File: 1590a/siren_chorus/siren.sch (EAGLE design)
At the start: 52 parts, among them IC1 NE5532, Q1 2N5457

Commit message: finished chorus and tremolo baords; other tweaks & polish
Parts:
- removed LED: PADSQR, supply pins:PADSQR
- added L+: PADSQR, supply pins:PADSQR
- added PAD1: PAD, supply pins:PAD
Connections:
- net LED: now also L+.P$1; no longer LED.P$1
- net VC: now also PAD1.P$1
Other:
- note added: "PT2399 CHORUS based on the madbean pedals glam (c)2016 burr settles"
- note added: "SIREN"
- moved on the sheet: 9V, BIAS, C1, C10, C11, C12, C13, C14, C15, C16, C17, C18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

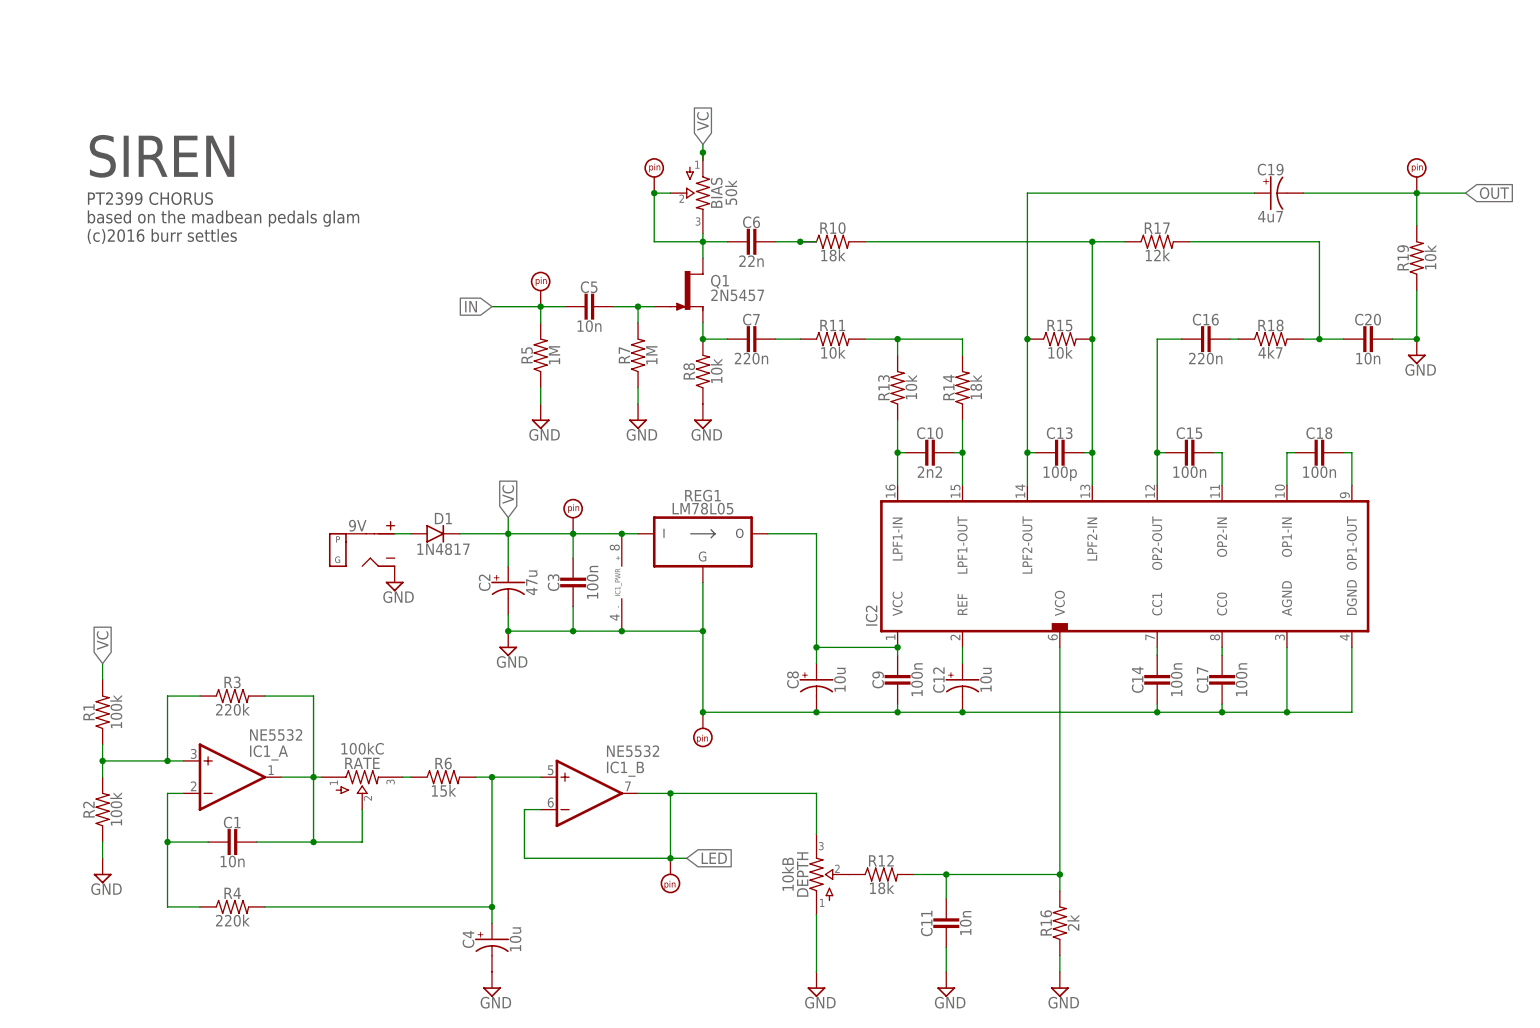
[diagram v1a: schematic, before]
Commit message: prettified schematics a bit
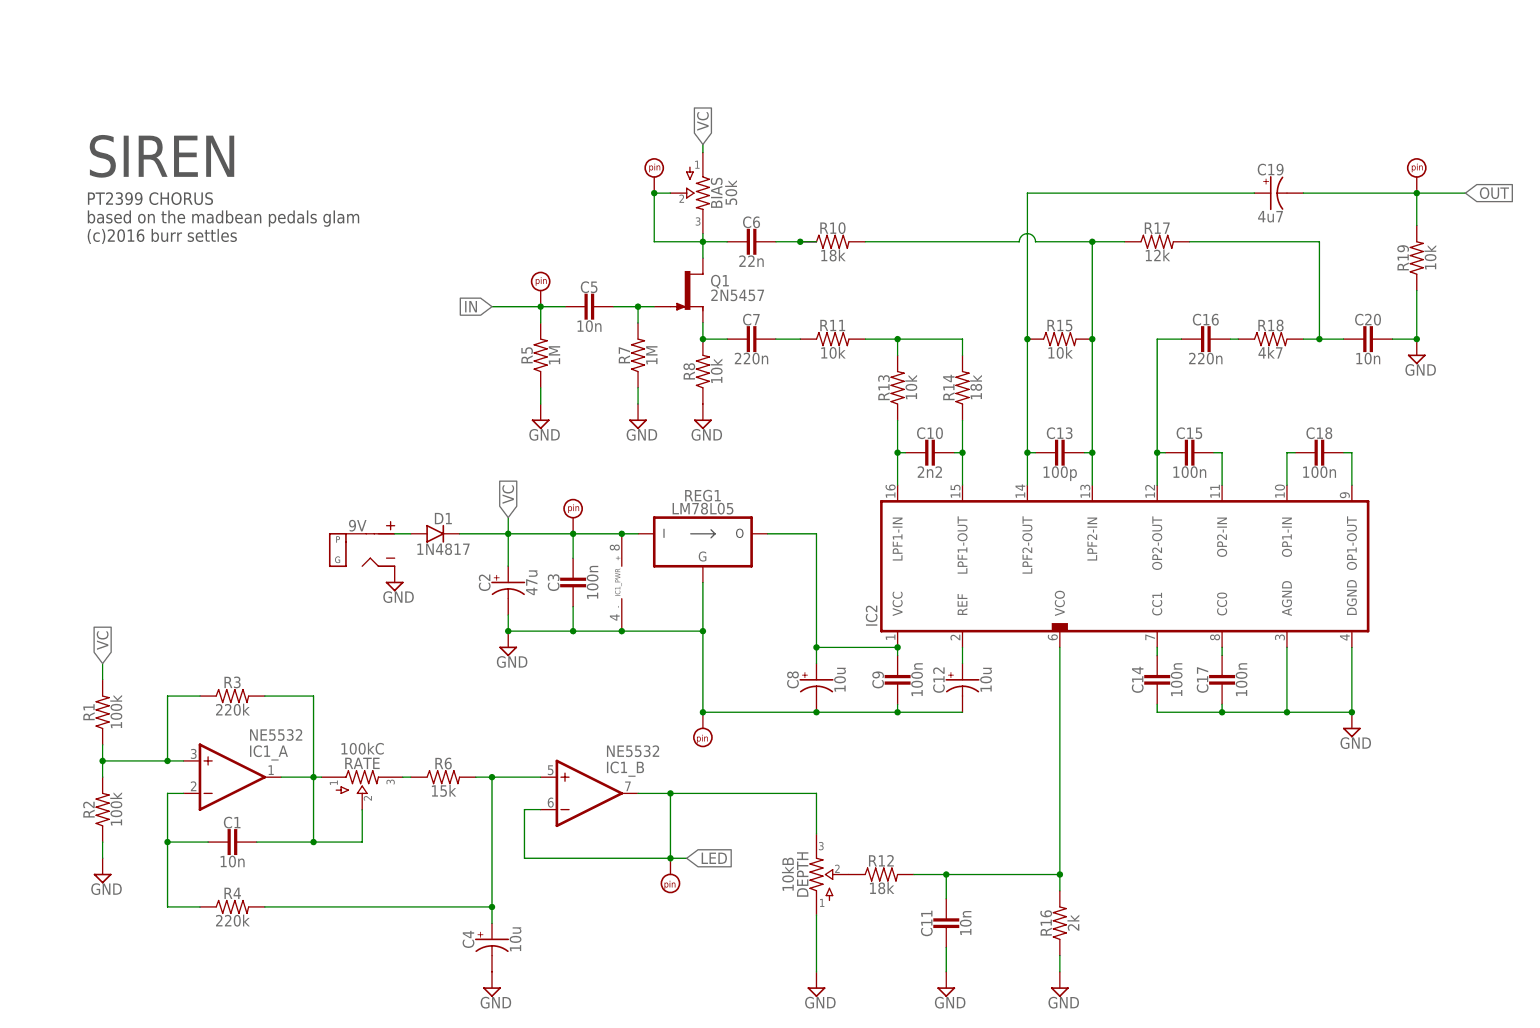
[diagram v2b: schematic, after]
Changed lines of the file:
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@@
 <setting verticaltext="up"/>
 </settings>
-<grid distance="0.1" unitdist="inch" unit="inch" style="lines" multiple="1" display="no" altdistance="0.01" altunitdist="inch" altunit="inch"/>
+<grid distance="0.05" unitdist="inch" unit="inch" style="lines" multiple="2" display="no" altdistance="0.01" altunitdist="inch" altunit="inch"/>
 <layers>
 <layer number="1" name="Top" color="4" fill="1" visible="no" active="no"/>
@@
 <part name="L+" library="supply pins" deviceset="PAD" device="SQR"/>
 <part name="PAD1" library="supply pins" deviceset="PAD" device=""/>
+<part name="GND8" library="supply pins" deviceset="GND" device=""/>
 </parts>
 <sheets>
@@
 <instance part="L+" gate="G$1" x="96.52" y="27.94" rot="R180"/>
 <instance part="PAD1" gate="G$1" x="81.28" y="78.74"/>
+<instance part="GND8" gate="GND" x="203.2" y="48.26"/>
 </instances>
 <busses>
@@
 <pinref part="C9" gate="G$1" pin="2"/>
 <wire x1="132.08" y1="52.07" x2="132.08" y2="50.8" width="0.1524" layer="91"/>
-<pinref part="IC2" gate="G$1" pin="DGND"/>
-<wire x1="142.24" y1="50.8" x2="172.72" y2="50.8" width="0.1524" layer="91"/>
-<wire x1="172.72" y1="50.8" x2="182.88" y2="50.8" width="0.1524" layer="91"/>
-<wire x1="182.88" y1="50.8" x2="193.04" y2="50.8" width="0.1524" layer="91"/>
-<wire x1="193.04" y1="50.8" x2="203.2" y2="50.8" width="0.1524" layer="91"/>
-<wire x1="203.2" y1="50.8" x2="203.2" y2="60.96" width="0.1524" layer="91"/>
-<junction x="142.24" y="50.8"/>
-<pinref part="IC2" gate="G$1" pin="AGND"/>
-<wire x1="193.04" y1="60.96" x2="193.04" y2="50.8" width="0.1524" layer="91"/>
-<junction x="193.04" y="50.8"/>
-<wire x1="182.88" y1="50.8" x2="182.88" y2="52.07" width="0.1524" layer="91"/>
-<junction x="182.88" y="50.8"/>
-<wire x1="172.72" y1="50.8" x2="172.72" y2="52.07" width="0.1524" layer="91"/>
-<junction x="172.72" y="50.8"/>
 <wire x1="88.9" y1="63.5" x2="101.6" y2="63.5" width="0.1524" layer="91"/>
 <junction x="88.9" y="63.5"/>
 <junction x="101.6" y="63.5"/>
 <junction x="71.12" y="63.5"/>
-<pinref part="C14" gate="G$1" pin="2"/>
-<pinref part="C17" gate="G$1" pin="2"/>
 <pinref part="GND" gate="G$1" pin="P$1"/>
 <junction x="101.6" y="50.8"/>
@@
 <pinref part="9V" gate="DC" pin="SLEEVE"/>
 <pinref part="GND3" gate="GND" pin="GND"/>
+</segment>
+<segment>
+<pinref part="IC2" gate="G$1" pin="DGND"/>
+<wire x1="203.2" y1="50.8" x2="203.2" y2="60.96" width="0.1524" layer="91"/>
+<pinref part="C17" gate="G$1" pin="2"/>
+<pinref part="C14" gate="G$1" pin="2"/>
+<wire x1="172.72" y1="50.8" x2="172.72" y2="52.07" width="0.1524" layer="91"/>
+<wire x1="172.72" y1="50.8" x2="182.88" y2="50.8" width="0.1524" layer="91"/>
+<wire x1="182.88" y1="50.8" x2="182.88" y2="52.07" width="0.1524" layer="91"/>
+<junction x="182.88" y="50.8"/>
+<wire x1="182.88" y1="50.8" x2="193.04" y2="50.8" width="0.1524" layer="91"/>
+<wire x1="193.04" y1="50.8" x2="203.2" y2="50.8" width="0.1524" layer="91"/>
+<junction x="193.04" y="50.8"/>
+<pinref part="IC2" gate="G$1" pin="AGND"/>
+<wire x1="193.04" y1="60.96" x2="193.04" y2="50.8" width="0.1524" layer="91"/>
+<pinref part="GND8" gate="GND" pin="GND"/>
+<junction x="203.2" y="50.8"/>
 </segment>
 </net>
@@
 </segment>
 <segment>
-<wire x1="101.6" y1="137.16" x2="101.6" y2="138.43" width="0.1524" layer="91"/>
 <label x="101.6" y="139.7" size="1.778" layer="95" rot="R90" xref="yes"/>
 <pinref part="BIAS" gate="G$1" pin="1"/>
 <wire x1="101.6" y1="138.43" x2="101.6" y2="139.7" width="0.1524" layer="91"/>
-<junction x="101.6" y="138.43"/>
 </segment>
 <segment>
@@
 <pinref part="R15" gate="G$1" pin="1"/>
 <junction x="152.4" y="109.22"/>
-</segment>
-</net>
-<net name="N$14" class="0">
-<segment>
-<pinref part="IC2" gate="G$1" pin="LPF2-IN"/>
-<wire x1="162.56" y1="86.36" x2="162.56" y2="91.44" width="0.1524" layer="91"/>
-<wire x1="162.56" y1="91.44" x2="162.56" y2="109.22" width="0.1524" layer="91"/>
-<junction x="162.56" y="91.44"/>
-<pinref part="C13" gate="G$1" pin="1"/>
-<wire x1="162.56" y1="109.22" x2="162.56" y2="124.46" width="0.1524" layer="91"/>
-<wire x1="161.29" y1="91.44" x2="162.56" y2="91.44" width="0.1524" layer="91"/>
-<pinref part="R10" gate="G$1" pin="2"/>
-<wire x1="127" y1="124.46" x2="162.56" y2="124.46" width="0.1524" layer="91"/>
-<wire x1="162.56" y1="124.46" x2="167.64" y2="124.46" width="0.1524" layer="91"/>
-<junction x="162.56" y="124.46"/>
-<pinref part="R17" gate="G$1" pin="1"/>
-<pinref part="R15" gate="G$1" pin="2"/>
-<junction x="162.56" y="109.22"/>
 </segment>
 </net>
@@
 </segment>
 </net>
+<net name="N$1" class="0">
+<segment>
+<pinref part="R17" gate="G$1" pin="1"/>
+<pinref part="R10" gate="G$1" pin="2"/>
+<wire x1="127" y1="124.46" x2="151.13" y2="124.46" width="0.1524" layer="91"/>
+<wire x1="151.13" y1="124.46" x2="153.67" y2="124.46" width="0.1524" layer="91" curve="-180" cap="flat"/>
+<wire x1="153.67" y1="124.46" x2="162.56" y2="124.46" width="0.1524" layer="91"/>
+<wire x1="162.56" y1="124.46" x2="167.64" y2="124.46" width="0.1524" layer="91"/>
+<junction x="162.56" y="124.46"/>
+<wire x1="162.56" y1="109.22" x2="162.56" y2="124.46" width="0.1524" layer="91"/>
+<pinref part="R15" gate="G$1" pin="2"/>
+<junction x="162.56" y="109.22"/>
+<pinref part="IC2" gate="G$1" pin="LPF2-IN"/>
+<wire x1="162.56" y1="86.36" x2="162.56" y2="91.44" width="0.1524" layer="91"/>
+<wire x1="162.56" y1="91.44" x2="162.56" y2="109.22" width="0.1524" layer="91"/>
+<junction x="162.56" y="91.44"/>
+<pinref part="C13" gate="G$1" pin="1"/>
+<wire x1="161.29" y1="91.44" x2="162.56" y2="91.44" width="0.1524" layer="91"/>
+</segment>
+</net>

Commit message: added RT logo; converted some pots trimmers
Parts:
- DEPTH: device potentiometers:POTSSMALL_PADS -> potentiometers:POTSTRIM
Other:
- note added: "PT2399 CHORUS based on the madbeanpedals glam (c)2016 burr settles"
- note removed: "PT2399 CHORUS based on the madbean pedals glam (c)2016 burr settles"
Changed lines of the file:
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@@
 <setting verticaltext="up"/>
 </settings>
-<grid distance="0.05" unitdist="inch" unit="inch" style="lines" multiple="2" display="no" altdistance="0.01" altunitdist="inch" altunit="inch"/>
+<grid distance="0.1" unitdist="inch" unit="inch" style="lines" multiple="1" display="no" altdistance="0.01" altunitdist="inch" altunit="inch"/>
 <layers>
 <layer number="1" name="Top" color="4" fill="1" visible="no" active="no"/>
@@
 <part name="C11" library="capacitors-film" deviceset="CER/FILM" device="2" value="10n"/>
 <part name="BIAS" library="potentiometers" deviceset="POTS" device="TRIM" value="50k"/>
-<part name="DEPTH" library="potentiometers" deviceset="POTS" device="SMALL_PADS" value="10kB"/>
+<part name="DEPTH" library="potentiometers" deviceset="POTS" device="TRIM" value="10kB"/>
 <part name="RATE" library="potentiometers" deviceset="POTS" device="SMALL_PADS" value="100kC"/>
 <part name="R19" library="resistors" deviceset="R_" device=".2" value="10k"/>
@@
 <part name="PAD1" library="supply pins" deviceset="PAD" device=""/>
 <part name="GND8" library="supply pins" deviceset="GND" device=""/>
+<part name="U$2" library="logos" deviceset="REBELSTRUST" device=""/>
 </parts>
 <sheets>
@@
 <plain>
 <text x="5.08" y="124.46" size="1.9304" layer="97">PT2399 CHORUS
-based on the madbean pedals glam
+based on the madbeanpedals glam
 (c)2016 burr settles</text>
 <text x="5.08" y="134.62" size="6.4516" layer="97">SIREN</text>
@@
 <instance part="PAD1" gate="G$1" x="81.28" y="78.74"/>
 <instance part="GND8" gate="GND" x="203.2" y="48.26"/>
+<instance part="U$2" gate="G$1" x="5.08" y="111.76"/>
 </instances>
 <busses>

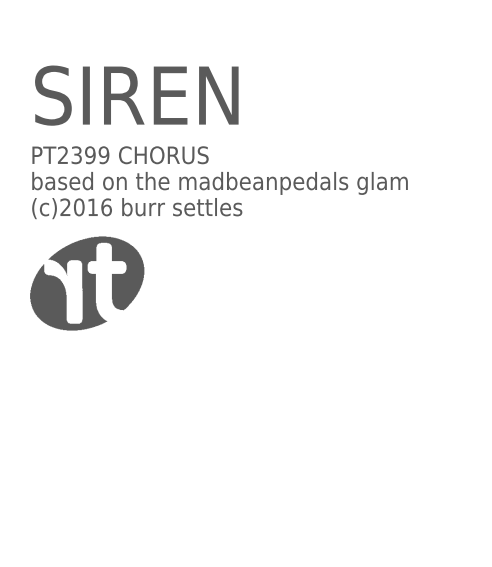
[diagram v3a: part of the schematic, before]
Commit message: convert bitmap logos to polygons
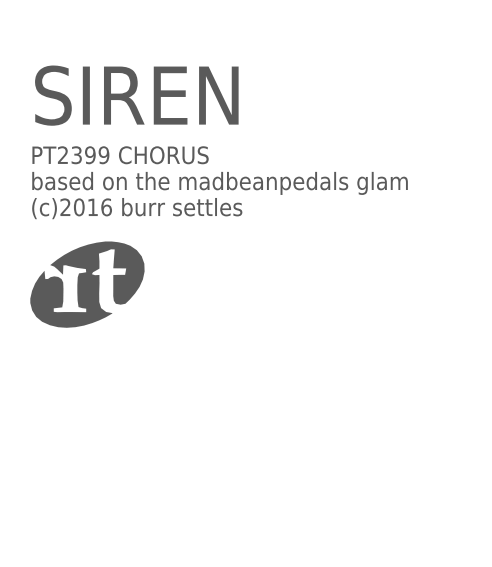
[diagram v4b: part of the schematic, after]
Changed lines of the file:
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@@
 <part name="PAD1" library="supply pins" deviceset="PAD" device=""/>
 <part name="GND8" library="supply pins" deviceset="GND" device=""/>
-<part name="U$2" library="logos" deviceset="REBELSTRUST" device=""/>
+<part name="U$1" library="logos" deviceset="REBELSTRUST" device=""/>
 </parts>
 <sheets>
@@
 <instance part="PAD1" gate="G$1" x="81.28" y="78.74"/>
 <instance part="GND8" gate="GND" x="203.2" y="48.26"/>
-<instance part="U$2" gate="G$1" x="5.08" y="111.76"/>
+<instance part="U$1" gate="G$1" x="5.08" y="111.76"/>
 </instances>
 <busses>
